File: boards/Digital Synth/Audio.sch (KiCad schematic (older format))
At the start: 36 parts, among them J1 AudioJack3, J2 AudioJack3, U2 PCM5101, U3 PCM5101A

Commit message: progress on layout for DAC and MIDI
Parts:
- removed C1, C12, C17, C3: 10u, symbol device:CP
- removed C10, C11: 2.2u, symbol device:C
- removed C13, C2, C6, C9: 0.1u, symbol device:C
- removed C15, C21: 2.2n, symbol device:C
- removed R1, R2: 470, symbol device:R
- removed U2: PCM5101, Package_SO:TSSOP-20_4.4x6.5mm_P0.65mm, symbol Audio:PCM5101
- C14, C16, C19, C20, C23, C24, C7, C8: footprint (none) -> Capacitor_SMD:C_0603_1608Metric_Pad1.05x0.95mm_HandSolder
- C18, C22, C4, C5: footprint (none) -> Capacitor_SMD:CP_Elec_4x5.8
- D1, D2, D3, D4: footprint (none) -> Diode_SMD:D_0805_2012Metric_Pad1.15x1.40mm_HandSolder
- J1, J2: footprint (none) -> Connector_Audio_Ext:Jack_6.35mm_Neutrik_NMJ4HFD2_Horizontal
- R3, R4: footprint (none) -> Resistor_SMD:R_0603_1608Metric_Pad1.05x0.95mm_HandSolder
- U3: footprint (none) -> Package_SO:TSSOP-20_4.4x6.5mm_P0.65mm
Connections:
- net labels removed: +3.3VA, GNDA, Lout, Rout, WS
- wire segments 168 -> 99
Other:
- moved on the sheet: C14, C16, C18, C19, C20, C22, C23, C24, C4, C5, C7, C8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

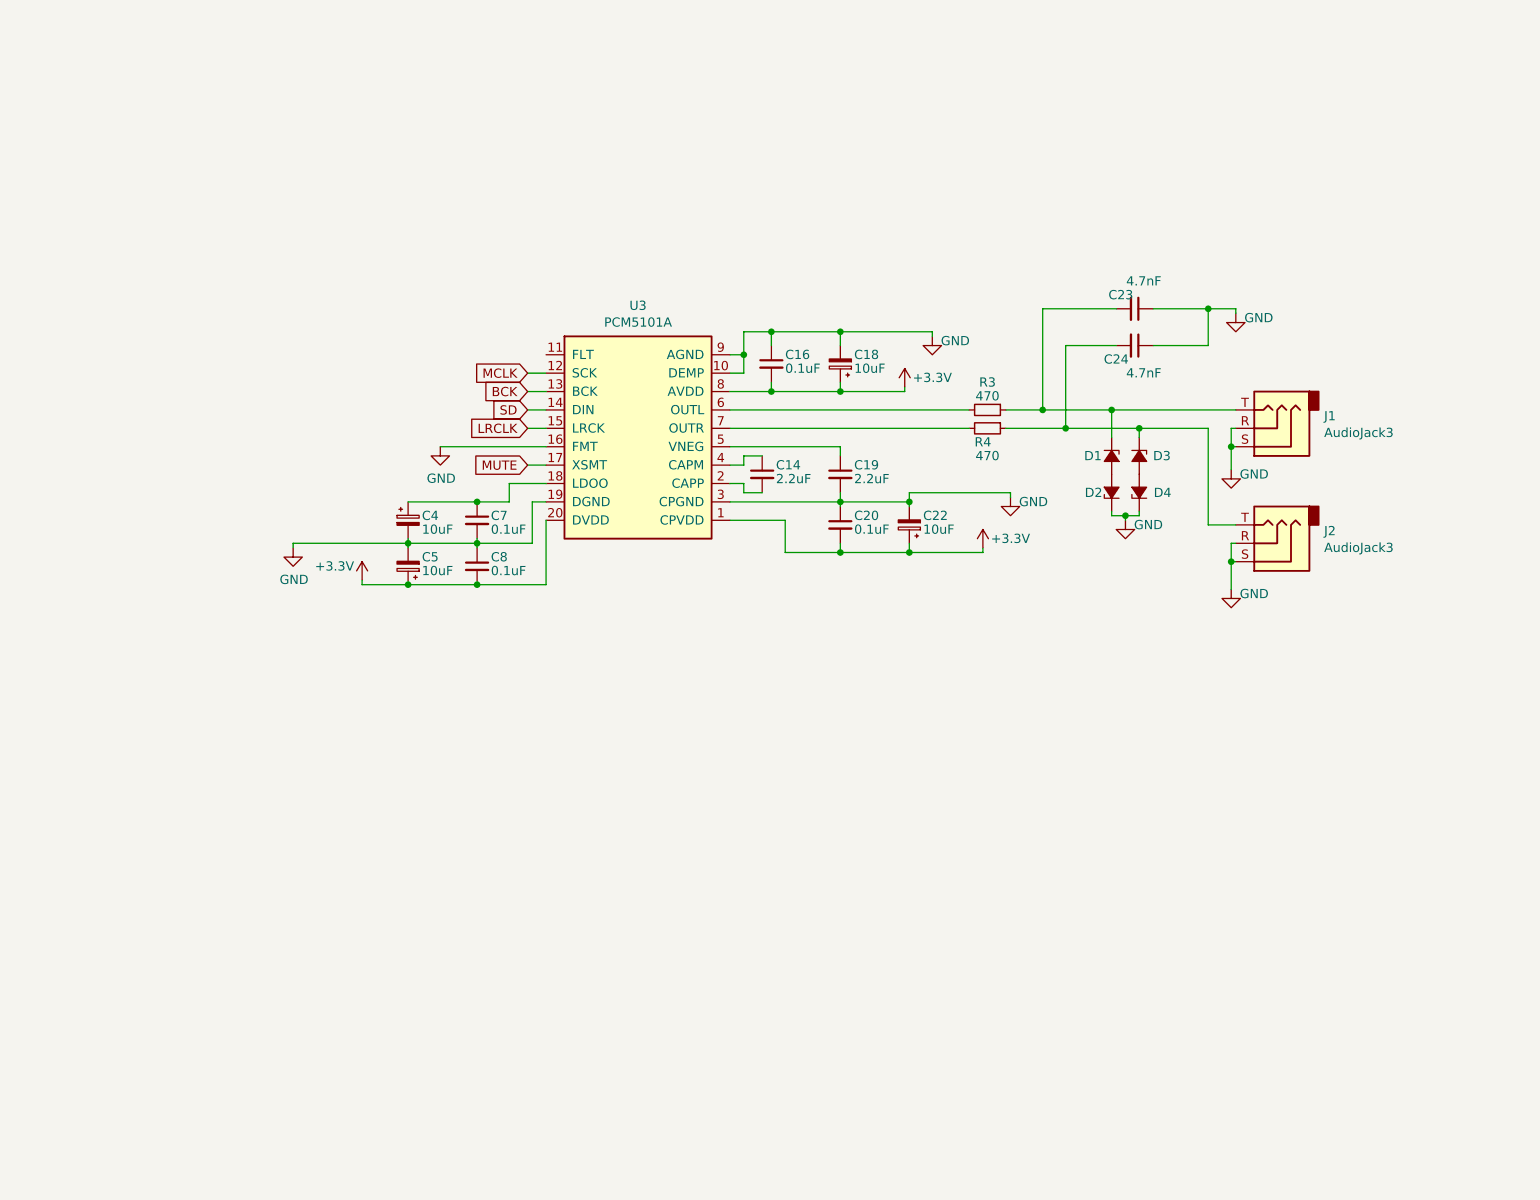
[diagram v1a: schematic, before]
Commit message: laid out keyboard
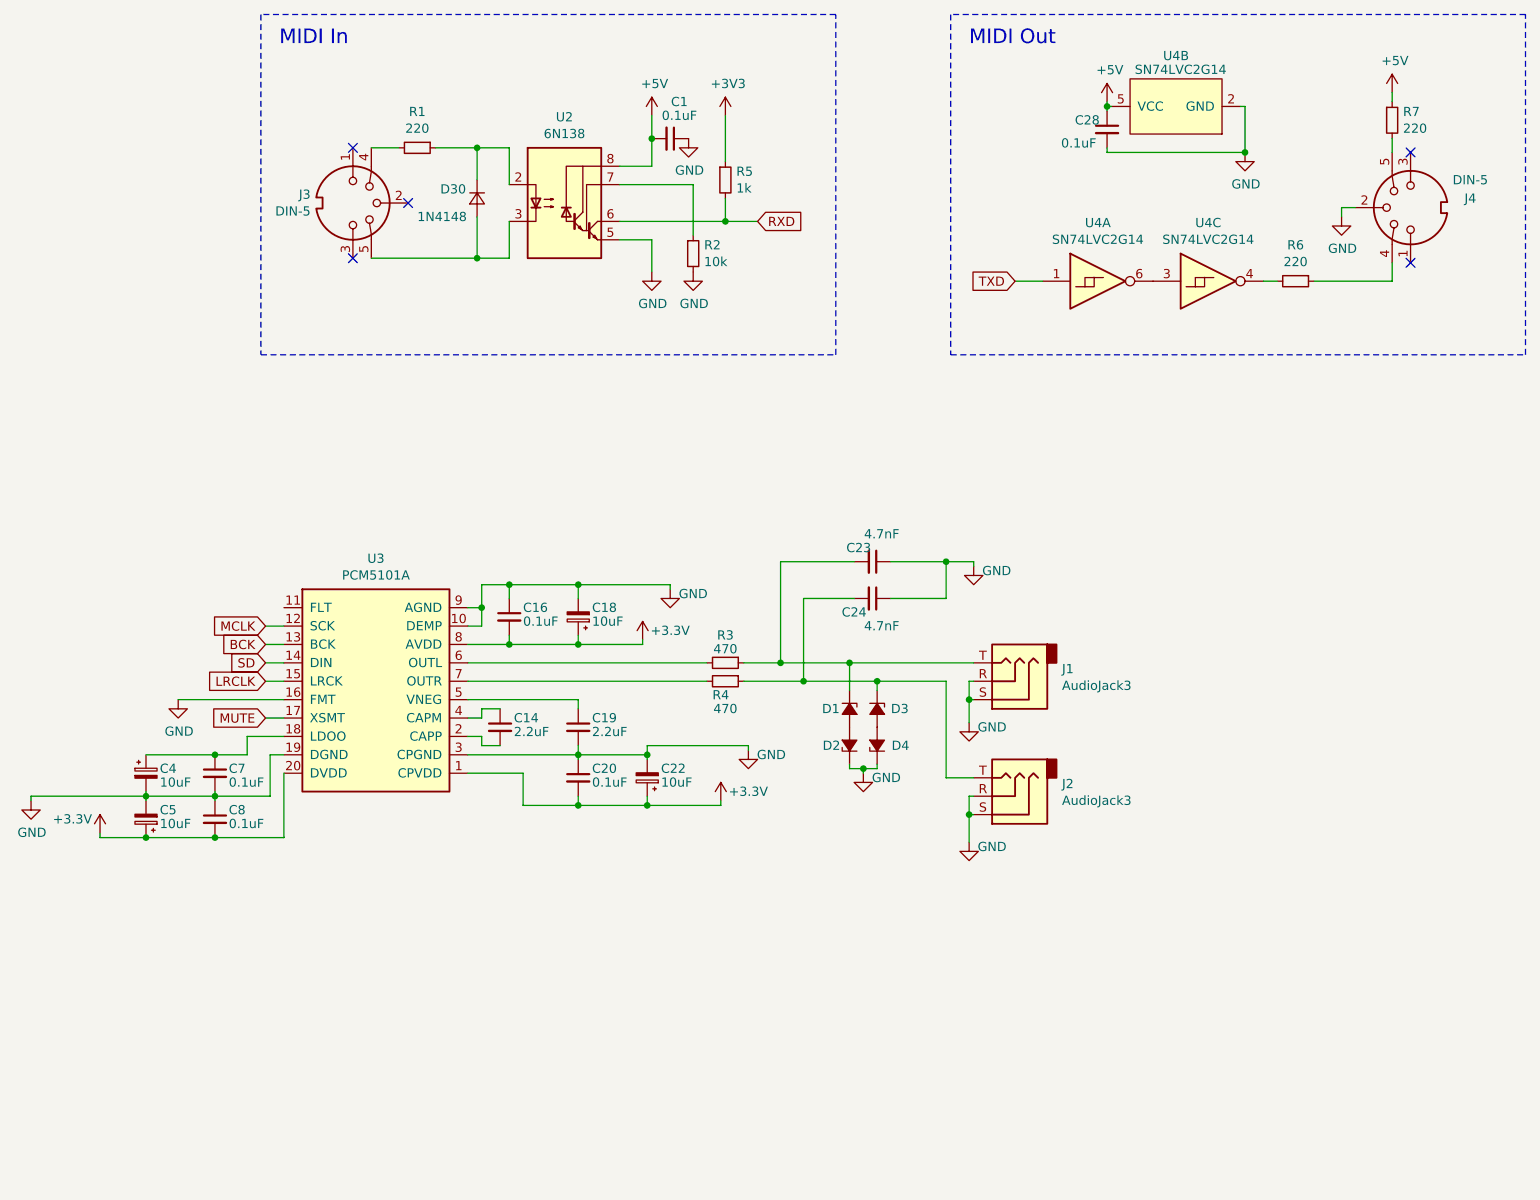
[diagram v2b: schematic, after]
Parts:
- added C1, C28: 0.1uF, Capacitor_SMD:C_0603_1608Metric_Pad1.05x0.95mm_HandSolder, symbol device:C_Small
- added D30: 1N4148, Diode_SMD:D_0805_2012Metric_Pad1.15x1.40mm_HandSolder, symbol device:D_Small
- added J3, J4: DIN-5, Connector_Audio_Ext:MIDI_DIN5, symbol Connector:DIN-5_180degree
- added R1, R6, R7: 220, Resistor_SMD:R_0805_2012Metric_Pad1.15x1.40mm_HandSolder, symbol device:R_Small
- added R2: 10k, Resistor_SMD:R_0805_2012Metric_Pad1.15x1.40mm_HandSolder, symbol device:R_Small
- added R5: 1k, Resistor_SMD:R_0805_2012Metric_Pad1.15x1.40mm_HandSolder, symbol device:R_Small
- added U2: 6N138, Package_DIP:SMDIP-8_W7.62mm, symbol Isolator:6N138
- added U4: SN74LVC2G14, Package_TO_SOT_SMD:SOT-23-6_Handsoldering, symbol 74xx:SN74LVC2G14
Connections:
- net +3V3: now also R5.1
- net GND: now also C1.1, C28.2, J4.2, R2.2, U2.5 (GND), U4.2 (GND)
- new net: J4.4, R6.1
- new net: R6.2, U4.4
- new net: J4.5, R7.2
- new net: U4.3, U4.6
- new net: D30.1 (K), R1.1, U2.2 (C1)
- new net: D30.2 (A), J3.5, U2.3 (C2)
- new net: J3.4, R1.2
- new net: R2.1, U2.7 (VO1)
- new net +5V: C1.2, C28.1, R7.1, U2.8 (VCC), U4.5 (VCC)
- new net RXD: R5.2, U2.6 (VO2)
- new net TXD: U4.1
- no-connect marks 0 -> 5
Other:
- note added: "MIDI In"
- note added: "MIDI Out"
- moved on the sheet: C14, C16, C18, C19, C20, C22, C23, C24, C4, C5, C7, C8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

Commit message: almost done with layout
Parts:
- removed D1, D2, D3, D4: D_Zener_Small_ALT, Diode_SMD:D_0805_2012Metric_Pad1.15x1.40mm_HandSolder, symbol device:D_Zener_Small_ALT
- removed J3, J4: DIN-5, Connector_Audio_Ext:MIDI_DIN5, symbol Connector:DIN-5_180degree
- added J3: MIDI IN, Connector_Audio:Jack_3.5mm_CUI_SJ1-3533NG_Horizontal, symbol Connector:AudioJack3
- added J4: MIDI OUT, Connector_Audio:Jack_3.5mm_CUI_SJ1-3533NG_Horizontal, symbol Connector:AudioJack3
- C23, C24: value 4.7nF -> 2.2nF; footprint Capacitor_SMD:C_0603_1608Metric_Pad1.05x0.95mm_HandSolder -> Capacitor_SMD:C_1206_3216Metric
- D30: footprint Diode_SMD:D_0805_2012Metric_Pad1.15x1.40mm_HandSolder -> Diode_SMD:D_SOD-323
- J1: value AudioJack3 -> LOUT; footprint Connector_Audio_Ext:Jack_6.35mm_Neutrik_NMJ4HFD2_Horizontal -> Connector_Audio:Jack_3.5mm_CUI_SJ1-3533NG_Horizontal
- J2: value AudioJack3 -> ROUT; footprint Connector_Audio_Ext:Jack_6.35mm_Neutrik_NMJ4HFD2_Horizontal -> Connector_Audio:Jack_3.5mm_CUI_SJ1-3533NG_Horizontal
- R1, R2, R5, R6, R7: footprint Resistor_SMD:R_0805_2012Metric_Pad1.15x1.40mm_HandSolder -> Resistor_SMD:R_0603_1608Metric_Pad1.05x0.95mm_HandSolder
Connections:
- net MUTE is gone; now on net +3V3: U3.17 (XSMT)
- net GND: now also U3.11 (FLT), J3.S, J4.S
- net at R6.1: now also J4.R
- net at R7.2: now also J4.T
- net at D30.2 (A), U2.3 (C2): now also J3.T
- net at R1.2: now also J3.R
- net RXD renamed RX_MIDI
- net TXD renamed TX_MIDI
- no-connect marks 5 -> 0
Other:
- note added: "DAC"
- moved on the sheet: C14, C16, C18, C19, C20, C22, C23, C24, C28, C4, C5, C7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

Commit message: finished layout
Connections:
- net MCLK renamed MCK
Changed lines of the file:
@@
 Comment4 ""
 $EndDescr
-Text GLabel 2700 4750 0    50   Input ~ 0
+Text GLabel 2800 4750 0    50   Input ~ 0
 SD
-Text GLabel 2700 4850 0    50   Input ~ 0
+Text GLabel 2800 4850 0    50   Input ~ 0
 LRCLK
-Text GLabel 2700 4650 0    50   Input ~ 0
+Text GLabel 2800 4650 0    50   Input ~ 0
 BCK
-Text GLabel 2700 4550 0    50   Input ~ 0
-MCLK
 Wire Wire Line
 	6525 5575 6525 5725
@@
 	1    0    0    -1
 $EndComp
-Wire Wire Line
-	2700 4850 2800 4850
-Wire Wire Line
-	2700 4750 2800 4750
-Wire Wire Line
-	2700 4650 2800 4650
-Wire Wire Line
-	2700 4550 2800 4550
 $Comp
 L Synth_Lib:PCM5101A U?
@@
 $EndComp
 Wire Wire Line
-	2800 4450 2225 4450
+	2800 4450 2350 4450
 $Comp
 L power:GND #PWR?
 U 1 1 6256264A
-P 2225 4475
+P 2350 4500
 AR Path="/6256264A" Ref="#PWR?"  Part="1"
 AR Path="/61FCD2FD/6256264A" Ref="#PWR0116"  Part="1"
-F 0 "#PWR0116" H 2225 4225 50  0001 C CNN
-F 1 "GND" H 2230 4302 50  0000 C CNN
-F 2 "" H 2225 4475 50  0001 C CNN
-F 3 "" H 2225 4475 50  0001 C CNN
-	1    2225 4475
-	1    0    0    -1
-$EndComp
-Wire Wire Line
-	2225 4450 2225 4475
+F 0 "#PWR0116" H 2350 4250 50  0001 C CNN
+F 1 "GND" H 2355 4327 50  0000 C CNN
+F 2 "" H 2350 4500 50  0001 C CNN
+F 3 "" H 2350 4500 50  0001 C CNN
+	1    2350 4500
+	1    0    0    -1
+$EndComp
+Wire Wire Line
+	2350 4450 2350 4500
+Text GLabel 2800 4550 0    50   Input ~ 0
+MCK
 $EndSCHEMATC
